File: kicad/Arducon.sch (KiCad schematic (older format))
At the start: 61 parts, among them J101 To Radio, J102 DB9 Female, J103 To Antenna, J104 Conn_01x08, J105 Conn_01x08, J106 Logic Level, J107 External Power Source, J108 Controlled Power, J109 Conn_01x01, J110 Conn_01x01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

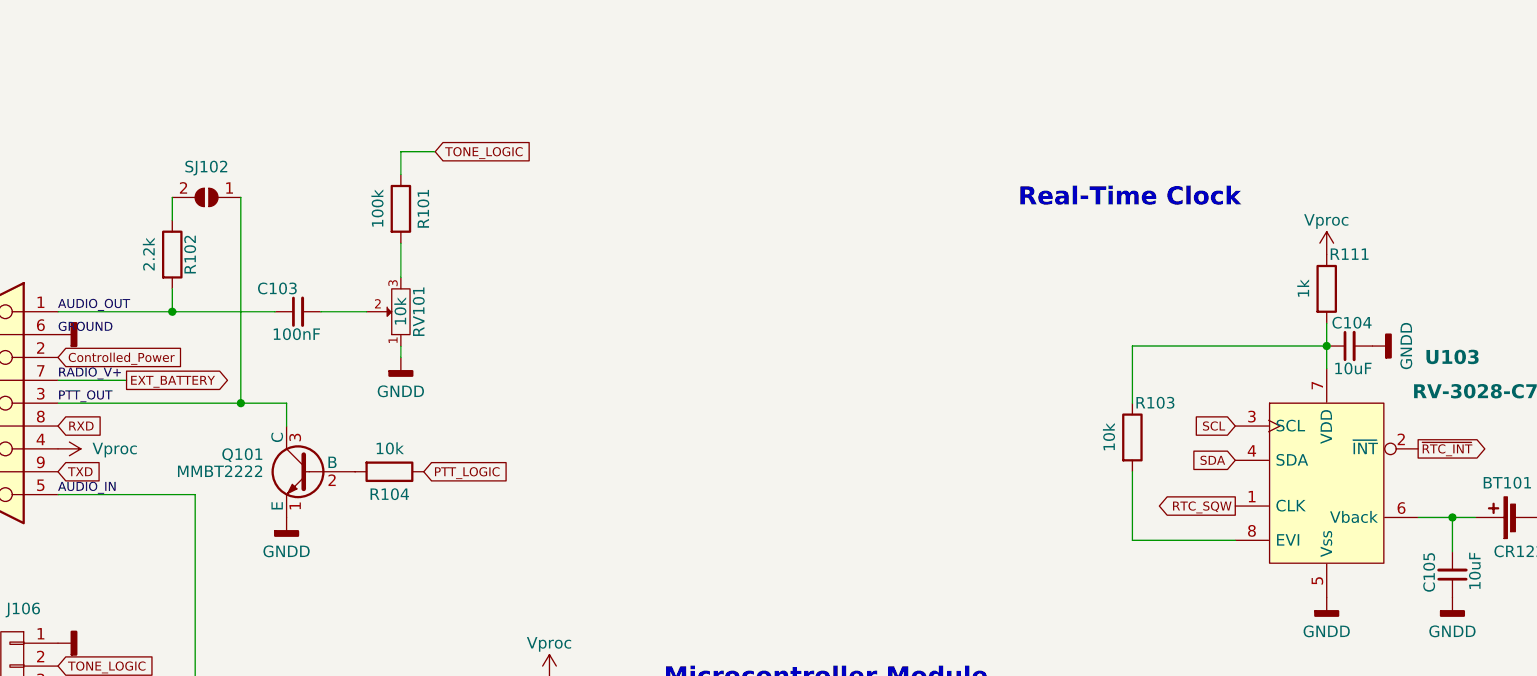
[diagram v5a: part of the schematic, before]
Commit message: PCB Updates
Added diode
Corrected transistor
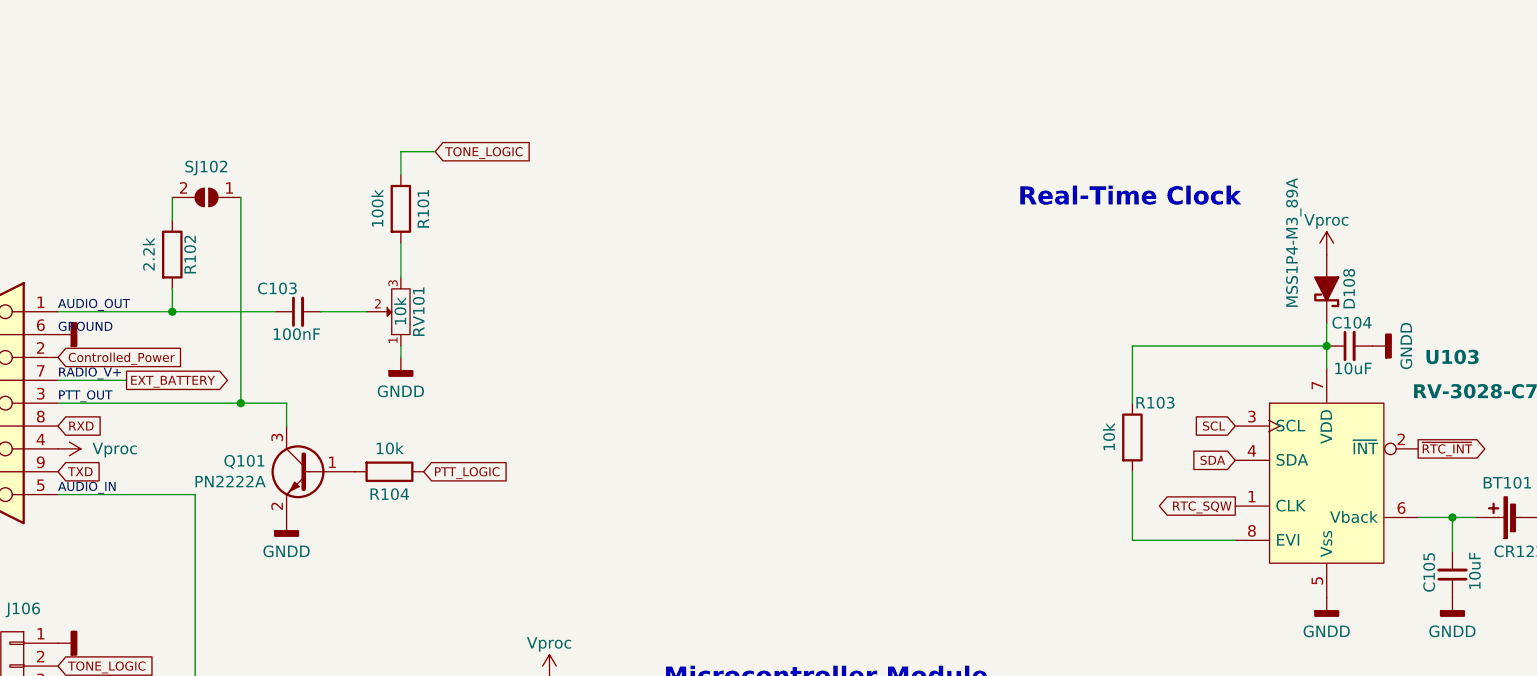
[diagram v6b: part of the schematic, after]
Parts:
- removed Q101: MMBT2222, TO_SOT_Packages_SMD:SOT-23, symbol Arducon-rescue:PN2222A
- removed R111: 1k, Resistors_SMD:R_0805, symbol Device:R
- added D108: MSS1P4-M3_89A, Diodes_SMD:DO-219AD, symbol Diode:MSS1P4-M3_89A
- added Q101: PN2222A, TO_SOT_Packages_SMD:SOT-23, symbol Transistor_BJT:PN2222A
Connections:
- net GND: now also Q101.2 (E)
- net PTT_OUT: now also Q101.3 (C)
- net Vproc: now also D108.2 (A)
- net at C104.1, R103.1, U103.7 (VDD): now also D108.1 (K)
- net at R104.2: now also Q101.1 (B)
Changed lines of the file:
@@
 Text Label 1800 2800 0    39   ~ 0
 GROUND
-$Comp
-L Arducon-rescue:PN2222A Q101
-U 1 1 5F9CFFCD
-P 2900 3400
-F 0 "Q101" H 3100 3475 50  0000 L CNN
-F 1 "MMBT2222" H 3100 3400 50  0000 L CNN
-F 2 "TO_SOT_Packages_SMD:SOT-23" H 3100 3325 50  0001 L CIN
-F 3 "" H 2900 3400 50  0001 L CNN
-F 4 "MMBT2222ATPMSCT-ND" H 2900 3400 50  0001 C CNN "Part No."
-F 5 "<a href=\"https://www.digikey.com/products/en?keywords=MMBT2222ATPMSCT-ND\">Link</a>" H 2900 3400 50  0001 C CNN "Link"
-	1    2900 3400
-	-1   0    0    -1
-$EndComp
 Wire Wire Line
 	1800 3100 2600 3100
@@
 	12150 6000 12150 850
 $Comp
-L Device:R R111
-U 1 1 600A7372
-P 7350 2600
-F 0 "R111" H 7450 2750 50  0000 C CNN
-F 1 "1k" V 7250 2600 50  0000 C CNN
-F 2 "Resistors_SMD:R_0805" H 7280 2600 50  0001 C CNN
-F 3 "" H 7350 2600 50  0001 C CNN
-F 4 "311-1.00KCRCT-ND" H 7350 2600 60  0001 C CNN "Part No."
-F 5 "<a href=\"https://www.digikey.com/products/en?keywords=311-1.00KCRCT-ND\">Link</a>" H 7350 2600 60  0001 C CNN "Link"
-	1    7350 2600
-	1    0    0    -1
-$EndComp
-$Comp
 L Device:C_Small C104
 U 1 1 60097870
@@
 	-1   0    0    1
 $EndComp
+$Comp
+L Diode:MSS1P4-M3_89A D108
+U 1 1 60344B01
+P 7350 2600
+F 0 "D108" H 7350 2700 50  0000 C CNN
+F 1 "MSS1P4-M3_89A" H 7550 2450 50  0000 C CNN
+F 2 "Diodes_SMD:DO-219AD" H 7350 2425 50  0001 C CNN
+F 3 "" H 7350 2600 50  0001 C CNN
+F 4 "MSS1P4-M3/89AGICT-ND" H 7350 2600 50  0001 C CNN "Part No."
+F 5 "<a href=\"https://www.digikey.com/products/en?keywords=MSS1P4-M3/89AGICT-ND\">Link</a>" H 7350 2600 50  0001 C CNN "Link"
+	1    7350 2600
+	0    1    -1   0
+$EndComp
+$Comp
+L Transistor_BJT:PN2222A Q101
+U 1 1 603D3C3C
+P 2900 3400
+F 0 "Q101" H 3091 3446 50  0000 L CNN
+F 1 "PN2222A" H 3091 3355 50  0000 L CNN
+F 2 "TO_SOT_Packages_SMD:SOT-23" H 3100 3325 50  0001 L CIN
+F 3 "" H 2900 3400 50  0001 L CNN
+F 4 "MMBT2222ATPMSCT-ND" H 2900 3400 50  0001 C CNN "Part No."
+F 5 "<a href=\"https://www.digikey.com/products/en?keywords=MMBT2222ATPMSCT-ND\">Link</a>" H 2900 3400 50  0001 C CNN "Link"
+	1    2900 3400
+	-1   0    0    -1
+$EndComp
 Wire Bus Line

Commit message: Schematic Update
PCB not yet updated
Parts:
- removed C105: 10uF, Capacitors_SMD:C_0805, symbol Device:C_Small
- removed D102: LED, LEDs:LED_0805, symbol Arducon-rescue:LED
- removed J106: Logic Level, Pin_Headers:Pin_Header_Straight_1x04, symbol Arducon-rescue:CONN_01X04
- added D109: MSS1P4-M3_89A, Diodes_SMD:DO-219AD, symbol Diode:MSS1P4-M3_89A
- added J106: Logic Level, symbol Connector_Generic:Conn_01x04
- added JP101, JP102: SolderJumper_3_Bridged12, Wire_Connections_Bridges:Solder-Jumperx3-NC_1-2_SMD-Pad_Small, symbol Jumper:SolderJumper_3_Bridged12
- added Q103: PN2222A, TO_SOT_Packages_SMD:SOT-23, symbol Transistor_BJT:PN2222A
- added R111: 10k, Resistors_SMD:R_0805, symbol Device:R
- J103: Link <a href=\"https://www.digikey.com/products/en?keywords=CON-SMA-EDGE-S-ND \">Link</a> -> <a href=\"https://www.digikey.com/products/en?keywords=CON-SMA-EDGE-S-ND\">Link</a>
- R109: value 470 -> 10k; Link <a href=\"https://www.digikey.com/products/en?keywords=311-470CRCT-ND\">Link</a> -> <a href=\"https://www.digikey.com/products/en?keywords=311-10.0KCRCT-ND\">Link</a>; Part No. 311-470CRCT-ND -> 311-10.0KCRCT-ND
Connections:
- net MISO is gone; now on net D4: MOD101.15 ((PCINT4/MISO)PB4), P101.6 (P6)
- net MOSI is gone; now on net D3: MOD101.14 ((PCINT3/OC2A/MOSI)PB3), P101.3 (P3)
- net PD5 is gone; now on net TONE_LOGIC: MOD101.8 ((PCINT21/OC0B/T1)PD5)
- net SCK is gone; now on net D5: MOD101.16 ((PCINT5/SCK)PB5), P101.4 (P4)
- net ADC7: now also R107.1; no longer R107.2
- net CW_KEY_LOGIC: now also MOD101.9 ((PCINT22/OC0A/AIN0)PD6), R109.1, JP101.1 (A); no longer MOD101.13 ((PCINT2/OC1B/~SS~)PB2)
- net D0: now also MOD101.11 ((PCINT0/CLKO/ICP1)PB0); no longer MOD101.17 ((PCINT8/ADC0)PC0)
- net D1: now also MOD101.12 ((PCINT1/OC1A)PB1); no longer MOD101.18 ((PCINT9/ADC1)PC1)
- net D2: now also MOD101.13 ((PCINT2/OC1B/~SS~)PB2); no longer MOD101.19 ((PCINT10/ADC2)PC2)
- net D3: no longer MOD101.20 ((PCINT11/ADC3)PC3)
- net D4: no longer D103.2 (A2), J102.8, MOD101.2 ((PCINT16/RXD)PD0)
- net D5: no longer MOD101.1 ((PCINT17/TXD)PD1), R110.1
- net EXT_BATTERY: now also JP102.1 (A); no longer R107.1
- net GND: now also J106.1 (Pin_1), Q103.2 (E), R111.2
- net PTT_LOGIC: now also MOD101.7 ((PCINT20/XCK/T0)PD4), J106.4 (Pin_4); no longer MOD101.11 ((PCINT0/CLKO/ICP1)PB0)
- net PWDN: now also MOD101.10 ((PCINT23/AIN1)PD7); no longer MOD101.9 ((PCINT22/OC0A/AIN0)PD6)
- net TONE_LOGIC: now also J106.2 (Pin_2); no longer MOD101.12 ((PCINT1/OC1A)PB1)
- net at BT101.1: now also D109.2 (A); no longer U103.6 (Vback)
- net at C104.1, D108.1 (K), R103.1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: now also D109.1 (K)
- net EXTERNAL_PWR_SOURCE: now reaches J107.2 (Pin_2), Q102.1 (E), SJ109.2 (B)
- net EXTERNAL_PWR_SOURCE: now also JP102.3 (B)
- net PD4 renamed PC3
- net PC3: now also MOD101.20 ((PCINT11/ADC3)PC3); no longer MOD101.7 ((PCINT20/XCK/T0)PD4)
- net PD7: no longer names the net of R109.2
- net PD7: now also Q103.1 (B); no longer MOD101.10 ((PCINT23/AIN1)PD7)
- new net: R111.1, U103.6 (Vback)
- new net: JP102.2 (C), R107.2
- new net: JP101.3 (B), Q103.3 (C)
- new net: J106.3 (Pin_3), JP101.2 (C)
- new net PC0: MOD101.17 ((PCINT8/ADC0)PC0)
- new net PC1: MOD101.18 ((PCINT9/ADC1)PC1)
- new net PC2: MOD101.19 ((PCINT10/ADC2)PC2)
- new net PD1: MOD101.1 ((PCINT17/TXD)PD1), R110.1
- new net RXD: D103.2 (A2), J102.8, MOD101.2 ((PCINT16/RXD)PD0)
- no-connect marks 11 -> 13
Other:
- moved on the sheet: BT101, C108, R105, R106, R107, R110, SW101

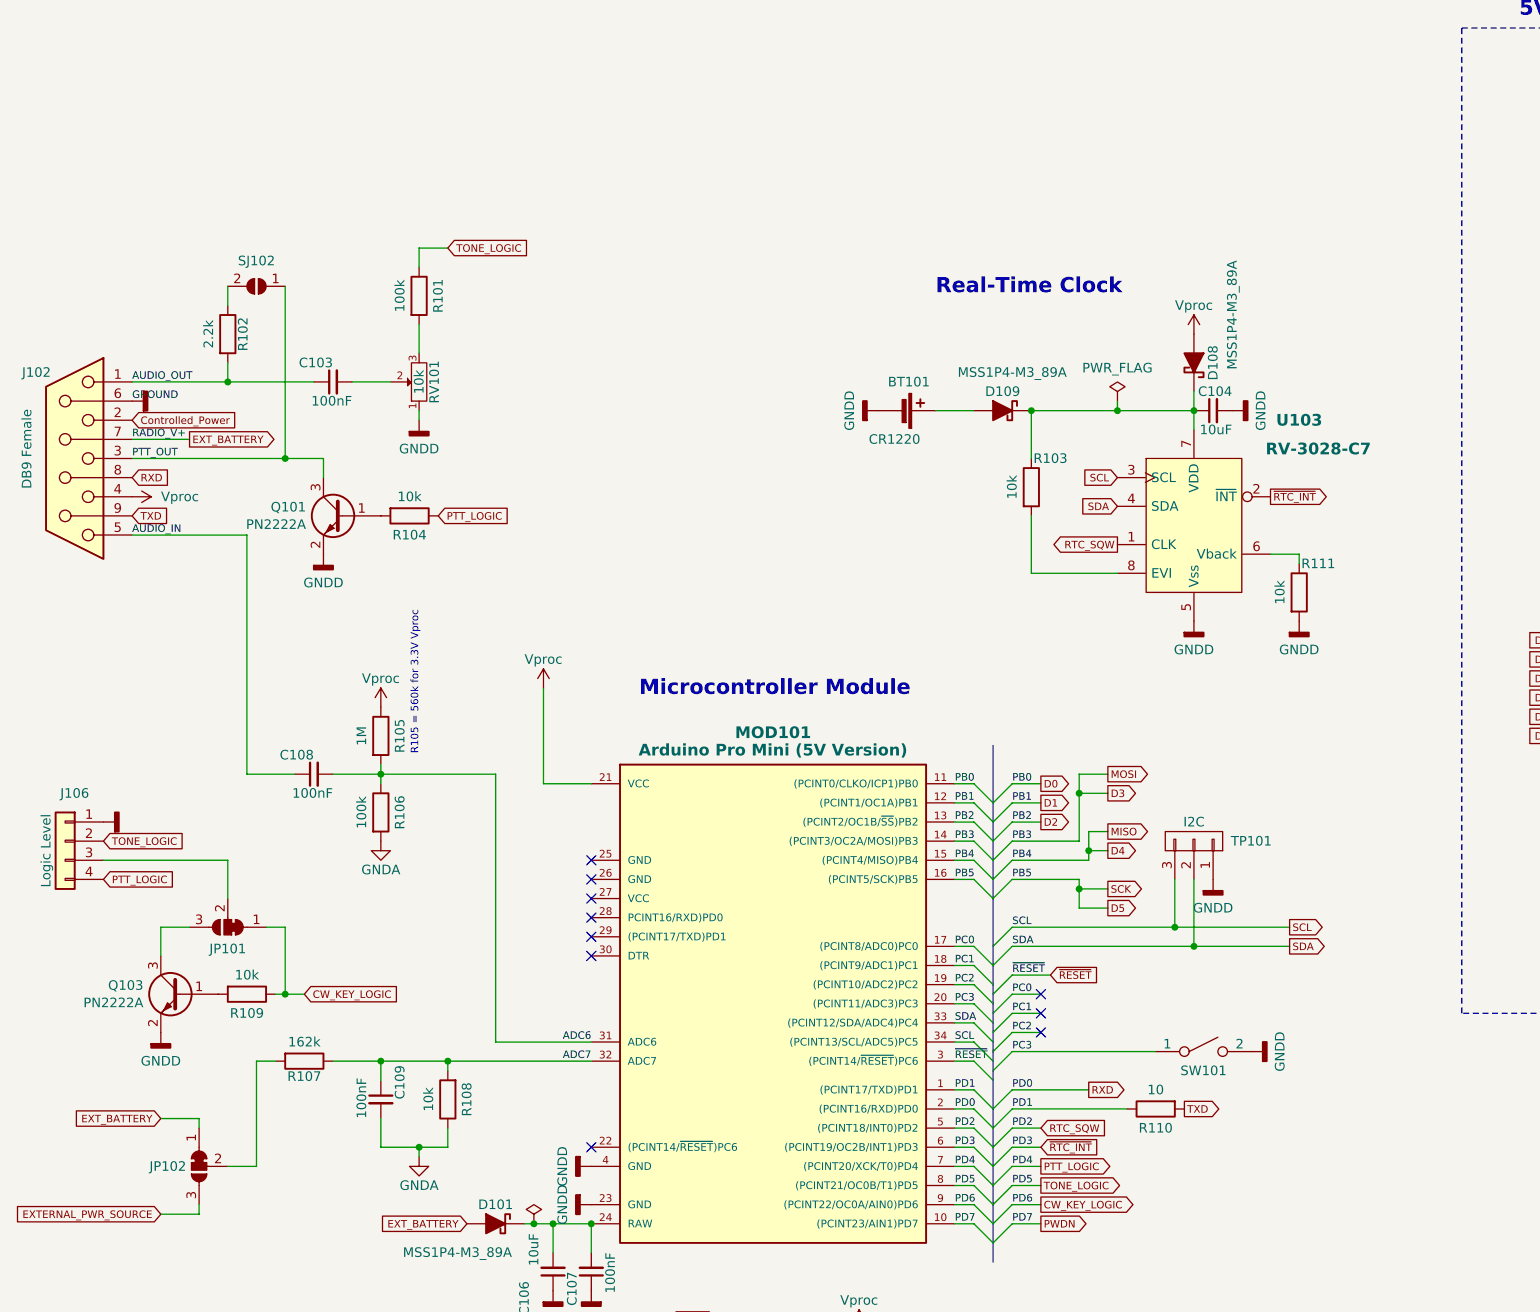
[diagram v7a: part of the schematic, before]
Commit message: Schematic & PCB Updates
Preparation for Version 2.0 hardware
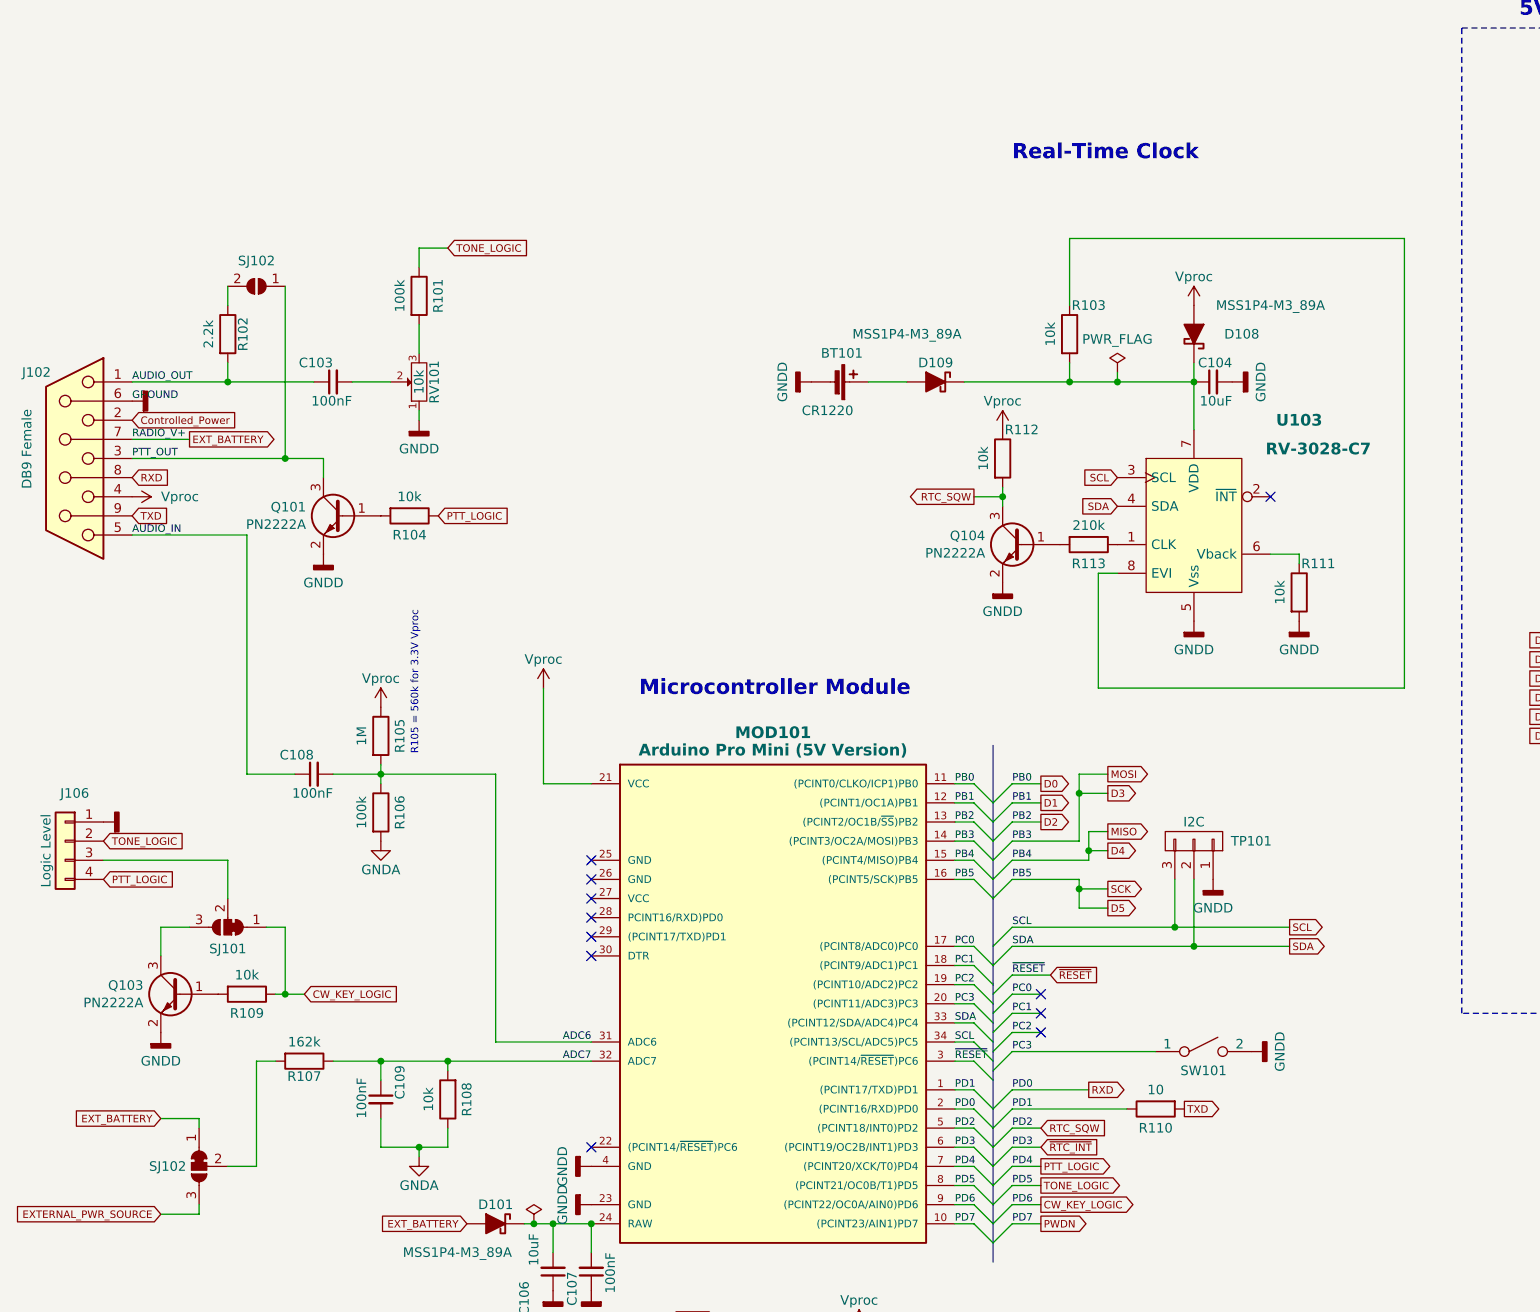
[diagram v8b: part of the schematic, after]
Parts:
- added Q104: PN2222A, TO_SOT_Packages_SMD:SOT-23, symbol Transistor_BJT:PN2222A
- added R112: 10k, Resistors_SMD:R_0805, symbol Device:R
- added R113: 210k, Resistors_SMD:R_0805, symbol Device:R
- J106: footprint (none) -> Pin_Headers:Pin_Header_Straight_1x04; Link (none) -> np; Part No. (none) -> np
- renumbered JP101 to SJ101, JP102 to SJ102
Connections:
- net GND: now also Q104.2 (E)
- net RTC_SQW: now also Q104.3 (C), R112.2; no longer U103.1 (CLK)
- net Vproc: now also R112.1
- net ~RTC_INT~: no longer U103.2 (~INT)
- net at C104.1, D108.1 (K), D109.1 (K)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: now also R103.2; no longer R103.1
- net at U103.8 (EVI): now also R103.1; no longer R103.2
- new net: R113.1, U103.1 (CLK)
- new net: Q104.1 (B), R113.2
- no-connect marks 13 -> 14
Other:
- moved on the sheet: BT101, C104, D108, D109, R103
